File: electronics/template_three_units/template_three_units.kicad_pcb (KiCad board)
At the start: 2 copper layers, 19 x 34 mm, 8 parts, among them J1 1, J2 2, J3 3, J4 4, J5 5, J6 6

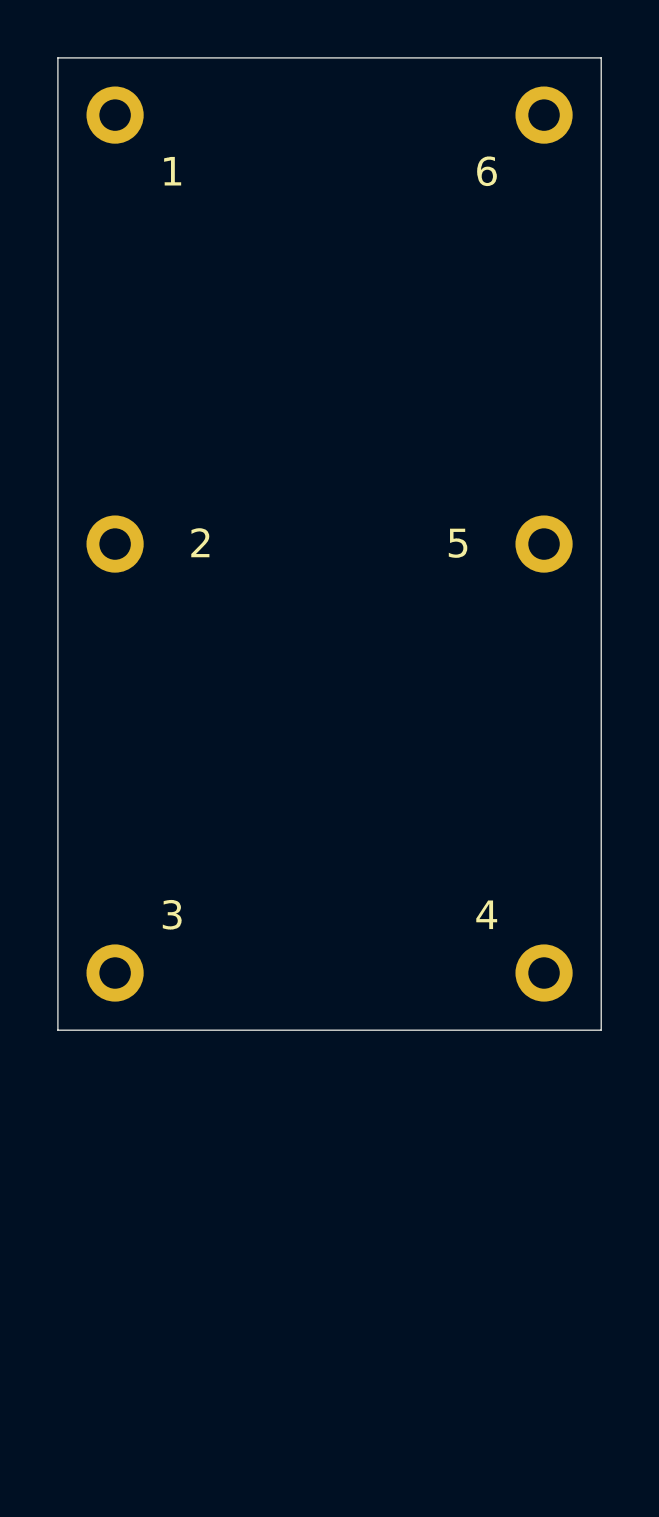
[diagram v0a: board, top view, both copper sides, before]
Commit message: added template for a three unit kosmos module
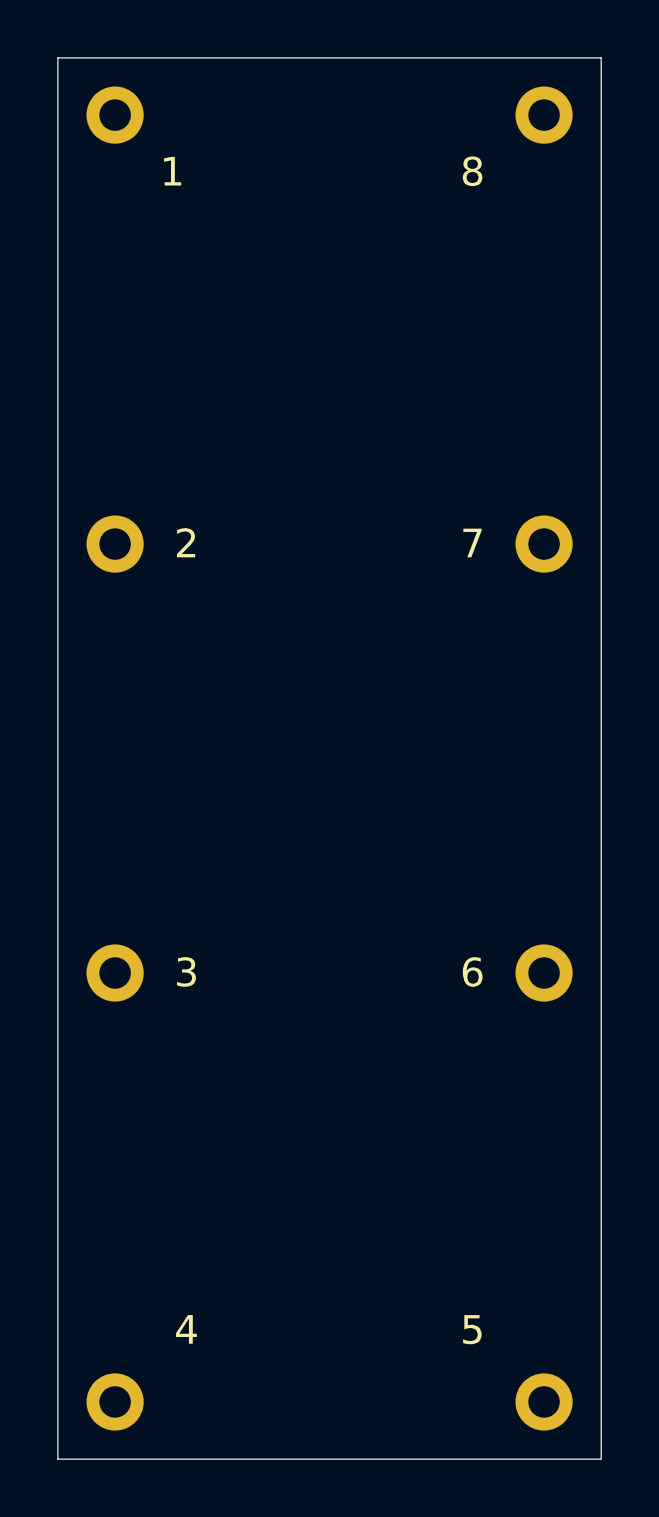
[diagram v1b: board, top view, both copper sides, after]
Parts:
- added J7: 7, mill-max:PC_pin_nail_head_6092, F.Cu at (157.0, 78.0)
- added J8: 8, mill-max:PC_pin_nail_head_6092, F.Cu at (157.0, 63.0)
- moved J5 30.0 mm to (157.0, 108.0)
- moved J6 30.0 mm to (157.0, 93.0)
- moved J4 21.2 mm to (142.0, 108.0)
- moved N1 6.50 mm to (149.0, 88.5)
- moved N2 6.50 mm to (150.0, 84.5)
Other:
- board size 19 x 34 mm -> 19 x 49 mm
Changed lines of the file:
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@@
     (tracks 0)
     (zones 0)
-    (modules 8)
+    (modules 10)
     (nets 2)
   )
@@
   (module mill-max:PC_pin_nail_head_6092 (layer F.Cu)
     (at 157 63)
-    (fp_text reference J6 (at -2 2) (layer F.Fab)
-      (effects (font (size 1 1) (thickness 0.15)))
-    )
-    (fp_text value 6 (at -2 2) (layer F.SilkS)
+    (fp_text reference J8 (at -2.5 2) (layer F.Fab)
+      (effects (font (size 1 1) (thickness 0.15)))
+    )
+    (fp_text value 8 (at -2.5 2) (layer F.SilkS)
       (effects (font (size 1 1) (thickness 0.15)))
     )
@@
   (module mill-max:PC_pin_nail_head_6092 (layer F.Cu)
     (at 157 78)
-    (fp_text reference J5 (at -3 0) (layer F.Fab)
-      (effects (font (size 1 1) (thickness 0.15)))
-    )
-    (fp_text value 5 (at -3 0) (layer F.SilkS)
-      (effects (font (size 1 1) (thickness 0.15)))
-    )
-    (fp_circle (center 0 0) (end 1.3 0) (layer F.CrtYd) (width 0.025))
-    (fp_circle (center 0 0) (end 1.3 0) (layer B.CrtYd) (width 0.025))
+    (fp_text reference J7 (at -2.5 0) (layer F.Fab)
+      (effects (font (size 1 1) (thickness 0.15)))
+    )
+    (fp_text value 7 (at -2.5 0) (layer F.SilkS)
+      (effects (font (size 1 1) (thickness 0.15)))
+    )
+    (fp_circle (center 0 0) (end 1.3 0) (layer F.CrtYd) (width 0.025))
+    (fp_circle (center 0 0) (end 1.3 0) (layer B.CrtYd) (width 0.025))
+    (pad 1 thru_hole circle (at 0 0) (size 2 2) (drill 1.1) (layers *.Cu *.Mask)
+      (net 1 "Net-(J1-Pad1)"))
+  )
+  (module mill-max:PC_pin_nail_head_6092 (layer F.Cu)
+    (at 157 93)
+    (fp_text reference J6 (at -2.5 0) (layer F.Fab)
+      (effects (font (size 1 1) (thickness 0.15)))
+    )
+    (fp_text value 6 (at -2.5 0) (layer F.SilkS)
+      (effects (font (size 1 1) (thickness 0.15)))
+    )
+    (fp_circle (center 0 0) (end 1.3 0) (layer B.CrtYd) (width 0.025))
+    (fp_circle (center 0 0) (end 1.3 0) (layer F.CrtYd) (width 0.025))
+    (pad 1 thru_hole circle (at 0 0) (size 2 2) (drill 1.1) (layers *.Cu *.Mask)
+      (net 1 "Net-(J1-Pad1)"))
+  )
+  (module mill-max:PC_pin_nail_head_6092 (layer F.Cu)
+    (at 157 108)
+    (fp_text reference J5 (at -2.5 -2.5) (layer F.Fab)
+      (effects (font (size 1 1) (thickness 0.15)))
+    )
+    (fp_text value 5 (at -2.5 -2.5) (layer F.SilkS)
+      (effects (font (size 1 1) (thickness 0.15)))
+    )
+    (fp_circle (center 0 0) (end 1.3 0) (layer B.CrtYd) (width 0.025))
+    (fp_circle (center 0 0) (end 1.3 0) (layer F.CrtYd) (width 0.025))
     (pad 1 thru_hole circle (at 0 0) (size 2 2) (drill 1.1) (layers *.Cu *.Mask)
       (net 1 "Net-(J1-Pad1)"))
   )
   (module mill-max:PC_pin_nail_head_6092 locked (layer F.Cu)
-    (at 157 93)
-    (fp_text reference J4 (at -2 -2) (layer F.Fab)
-      (effects (font (size 1 1) (thickness 0.15)))
-    )
-    (fp_text value 4 (at -2 -2) (layer F.SilkS)
-      (effects (font (size 1 1) (thickness 0.15)))
-    )
-    (fp_circle (center 0 0) (end 1.3 0) (layer B.CrtYd) (width 0.025))
-    (fp_circle (center 0 0) (end 1.3 0) (layer F.CrtYd) (width 0.025))
+    (at 142 108)
+    (fp_text reference J4 (at 2.5 -2.5) (layer F.Fab)
+      (effects (font (size 1 1) (thickness 0.15)))
+    )
+    (fp_text value 4 (at 2.5 -2.5) (layer F.SilkS)
+      (effects (font (size 1 1) (thickness 0.15)))
+    )
+    (fp_circle (center 0 0) (end 1.3 0) (layer F.CrtYd) (width 0.025))
+    (fp_circle (center 0 0) (end 1.3 0) (layer B.CrtYd) (width 0.025))
     (pad 1 thru_hole circle (at 0 0) (size 2 2) (drill 1.1) (layers *.Cu *.Mask)
       (net 1 "Net-(J1-Pad1)"))
@@
   (module mill-max:PC_pin_nail_head_6092 locked (layer F.Cu)
     (at 142 93)
-    (fp_text reference J3 (at 2 -2) (layer F.Fab)
-      (effects (font (size 1 1) (thickness 0.15)))
-    )
-    (fp_text value 3 (at 2 -2) (layer F.SilkS)
-      (effects (font (size 1 1) (thickness 0.15)))
-    )
-    (fp_circle (center 0 0) (end 1.3 0) (layer B.CrtYd) (width 0.025))
-    (fp_circle (center 0 0) (end 1.3 0) (layer F.CrtYd) (width 0.025))
+    (fp_text reference J3 (at 2.5 0) (layer F.Fab)
+      (effects (font (size 1 1) (thickness 0.15)))
+    )
+    (fp_text value 3 (at 2.5 0) (layer F.SilkS)
+      (effects (font (size 1 1) (thickness 0.15)))
+    )
+    (fp_circle (center 0 0) (end 1.3 0) (layer F.CrtYd) (width 0.025))
+    (fp_circle (center 0 0) (end 1.3 0) (layer B.CrtYd) (width 0.025))
     (pad 1 thru_hole circle (at 0 0) (size 2 2) (drill 1.1) (layers *.Cu *.Mask)
       (net 1 "Net-(J1-Pad1)"))
@@
   (module mill-max:PC_pin_nail_head_6092 locked (layer F.Cu)
     (at 142 78)
-    (fp_text reference J2 (at 3 0) (layer F.Fab)
-      (effects (font (size 1 1) (thickness 0.15)))
-    )
-    (fp_text value 2 (at 3 0) (layer F.SilkS)
-      (effects (font (size 1 1) (thickness 0.15)))
-    )
-    (fp_circle (center 0 0) (end 1.3 0) (layer B.CrtYd) (width 0.025))
-    (fp_circle (center 0 0) (end 1.3 0) (layer F.CrtYd) (width 0.025))
+    (fp_text reference J2 (at 2.5 0) (layer F.Fab)
+      (effects (font (size 1 1) (thickness 0.15)))
+    )
+    (fp_text value 2 (at 2.5 0) (layer F.SilkS)
+      (effects (font (size 1 1) (thickness 0.15)))
+    )
+    (fp_circle (center 0 0) (end 1.3 0) (layer F.CrtYd) (width 0.025))
+    (fp_circle (center 0 0) (end 1.3 0) (layer B.CrtYd) (width 0.025))
     (pad 1 thru_hole circle (at 0 0) (size 2 2) (drill 1.1) (layers *.Cu *.Mask)
       (net 1 "Net-(J1-Pad1)"))
@@
       (effects (font (size 1 1) (thickness 0.15)))
     )
-    (fp_circle (center 0 0) (end 1.3 0) (layer B.CrtYd) (width 0.025))
-    (fp_circle (center 0 0) (end 1.3 0) (layer F.CrtYd) (width 0.025))
+    (fp_circle (center 0 0) (end 1.3 0) (layer F.CrtYd) (width 0.025))
+    (fp_circle (center 0 0) (end 1.3 0) (layer B.CrtYd) (width 0.025))
     (pad 1 thru_hole circle (at 0 0) (size 2 2) (drill 1.1) (layers *.Cu *.Mask)
       (net 1 "Net-(J1-Pad1)"))
   )
   (module Symbol:OSHW-Symbol_6.7x6mm_SilkScreen (layer B.Cu)
-    (at 150 78 180)
+    (at 150 84.5 180)
     (descr "Open Source Hardware Symbol")
     (tags "Logo Symbol OSHW")
@@
   )
   (module SquantorLabels:Label_Generic (layer B.Cu)
-    (at 149 82)
+    (at 149 88.5)
     (descr "Label for general purpose use")
     (tags Label)
@@
   )
   (gr_line (start 159 61) (end 140 61) (layer Edge.Cuts) (width 0.05))
-  (gr_line (start 159 61) (end 159 95) (layer Edge.Cuts) (width 0.05))
-  (gr_line (start 140 95) (end 159 95) (layer Edge.Cuts) (width 0.05))
-  (gr_line (start 140 95) (end 140 61) (layer Edge.Cuts) (width 0.05))
+  (gr_line (start 159 61) (end 159 110) (layer Edge.Cuts) (width 0.05))
+  (gr_line (start 140 110) (end 159 110) (layer Edge.Cuts) (width 0.05))
+  (gr_line (start 140 110) (end 140 61) (layer Edge.Cuts) (width 0.05))
 )
